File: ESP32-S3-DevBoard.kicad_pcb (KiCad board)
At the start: 4 copper layers, 32 x 57.1 mm, 27 parts, among them J1 USB_C_Receptacle_USB2.0_14P, J2 Conn_01x22_Socket, J3 Conn_01x22_Socket, SW1 SW_Push, SW2 SW_Push, U1 ESP32-S3-WROOM-1, U2 AMS1117-3.3

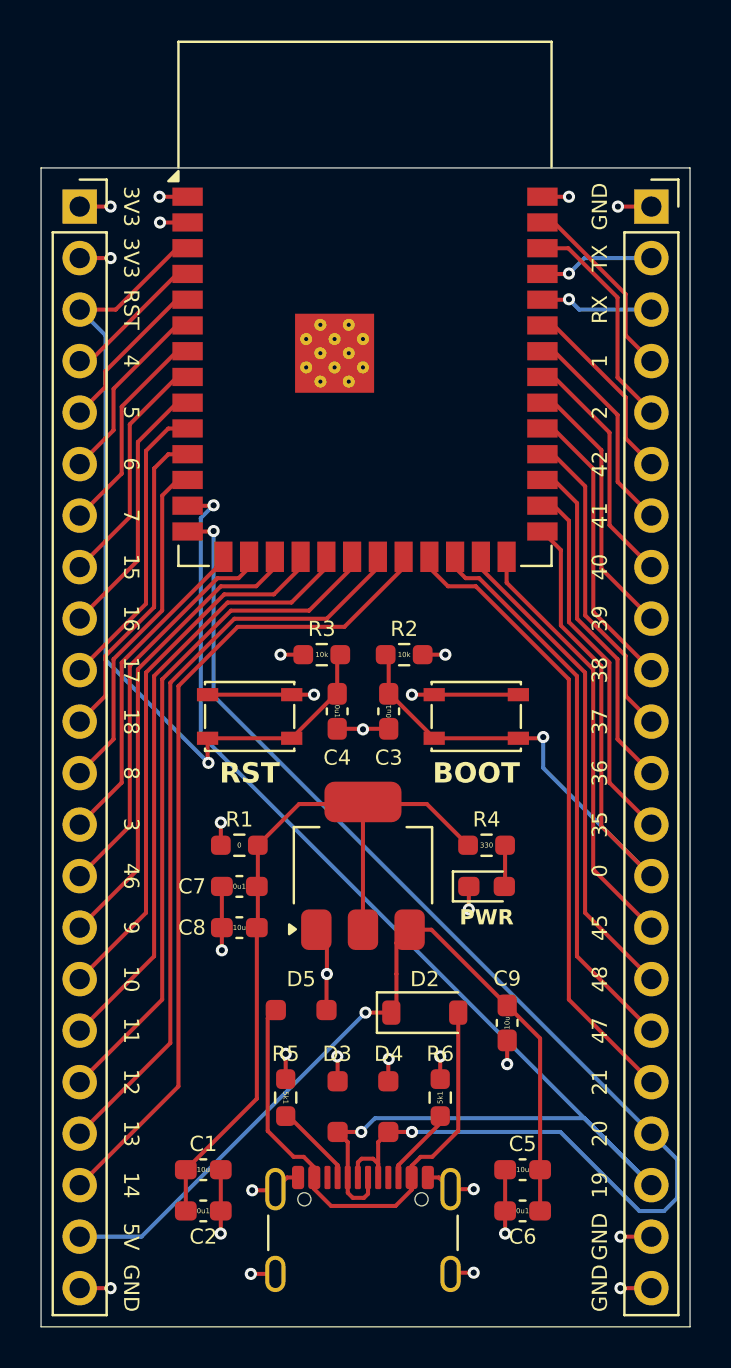
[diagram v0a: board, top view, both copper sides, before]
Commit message: Add impedance matching for USB lines
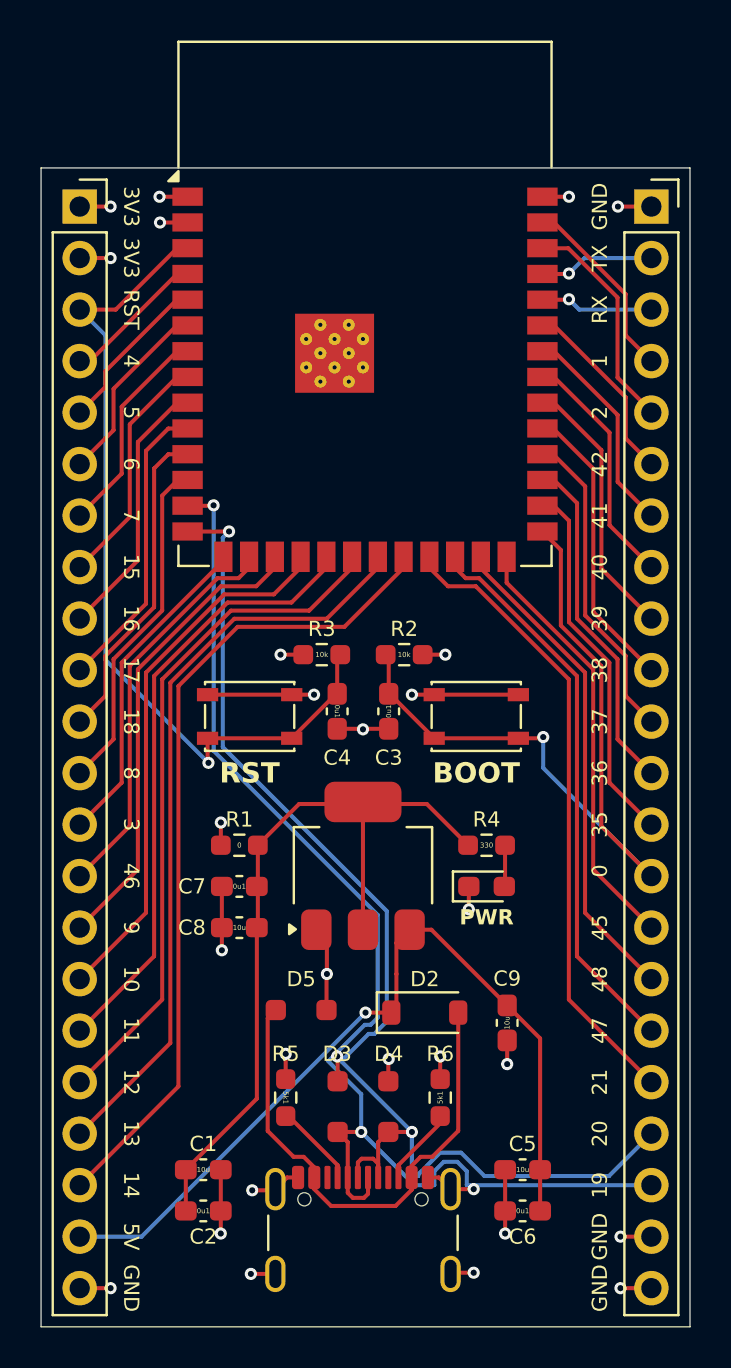
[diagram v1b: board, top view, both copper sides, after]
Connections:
- net GPIO_19 renamed D-
- net GPIO_20 renamed D+
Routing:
- net D-: track 66.6 -> 60.9 mm
- net D+: track 64.8 -> 59.6 mm
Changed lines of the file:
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@@
 	(net 42 "GPIO_21")
 	(net 43 "GPIO_47")
-	(net 44 "GPIO_19")
-	(net 45 "GPIO_20")
+	(net 44 "D-")
+	(net 45 "D+")
 	(footprint "Resistor_SMD:R_0603_1608Metric_Pad0.98x0.95mm_HandSolder"
 		(layer "F.Cu")
@@
 			(size 1.5 0.9)
 			(layers "F.Cu" "F.Paste" "F.Mask")
-			(net 44 "GPIO_19")
+			(net 44 "D-")
 			(pinfunction "IO19")
 			(pintype "bidirectional")
@@
 			(size 1.5 0.9)
 			(layers "F.Cu" "F.Paste" "F.Mask")
-			(net 45 "GPIO_20")
+			(net 45 "D+")
 			(pinfunction "IO20")
 			(pintype "bidirectional")
@@
 			(layers "*.Cu" "*.Mask")
 			(remove_unused_layers no)
-			(net 45 "GPIO_20")
+			(net 45 "D+")
 			(pinfunction "Pin_19")
 			(pintype "passive")
@@
 			(layers "*.Cu" "*.Mask")
 			(remove_unused_layers no)
-			(net 44 "GPIO_19")
+			(net 44 "D-")
 			(pinfunction "Pin_20")
 			(pintype "passive")
@@
 			(layers "F.Cu" "F.Paste" "F.Mask")
 			(roundrect_rratio 0.25)
-			(net 45 "GPIO_20")
+			(net 45 "D+")
 			(pinfunction "D+")
 			(pintype "bidirectional")
@@
 			(layers "F.Cu" "F.Paste" "F.Mask")
 			(roundrect_rratio 0.25)
-			(net 44 "GPIO_19")
+			(net 44 "D-")
 			(pinfunction "D-")
 			(pintype "bidirectional")
@@
 			(layers "F.Cu" "F.Paste" "F.Mask")
 			(roundrect_rratio 0.25)
-			(net 45 "GPIO_20")
+			(net 45 "D+")
 			(pinfunction "D+")
 			(pintype "bidirectional")
@@
 			(layers "F.Cu" "F.Paste" "F.Mask")
 			(roundrect_rratio 0.25)
-			(net 44 "GPIO_19")
+			(net 44 "D-")
 			(pinfunction "D-")
 			(pintype "bidirectional")
@@
 			(layers "F.Cu" "F.Paste" "F.Mask")
 			(roundrect_rratio 0.25)
-			(net 45 "GPIO_20")
+			(net 45 "D+")
 			(pinfunction "A1")
 			(pintype "passive")
@@
 			(layers "F.Cu" "F.Paste" "F.Mask")
 			(roundrect_rratio 0.25)
-			(net 44 "GPIO_19")
+			(net 44 "D-")
 			(pinfunction "A2")
 			(pintype "passive")
@@
 	)
 	(segment
-		(start 183.134 69.596)
-		(end 182.499 70.231)
+		(start 191.227 94.863529)
+		(end 190.875529 95.215)
 		(width 0.2)
 		(layer "B.Cu")
@@
 	)
 	(segment
-		(start 191.094 99.822)
-		(end 201.422 99.822)
+		(start 183.134 81.701471)
+		(end 191.227 89.794471)
 		(width 0.2)
 		(layer "B.Cu")
@@
 	)
 	(segment
-		(start 182.499 80.899)
-		(end 204.724 103.124)
+		(start 190.416 98.639397)
+		(end 190.416 100.5)
 		(width 0.2)
 		(layer "B.Cu")
@@
 	)
 	(segment
-		(start 201.422 99.822)
-		(end 204.724 103.124)
+		(start 193.04 103.124)
+		(end 194.02 103.124)
+		(width 0.2)
+		(layer "B.Cu")
+		(net 44)
+	)
+	(segment
+		(start 194.488629 101.971)
+		(end 195.151371 101.971)
 		(width 0.2)
 		(layer "B.Cu")
@@
 	)
 	(segment
-		(start 182.499 70.231)
-		(end 182.499 80.899)
+		(start 194.02 103.124)
+		(end 194.02 102.439629)
+		(width 0.2)
+		(layer "B.Cu")
+		(net 44)
+	)
+	(segment
+		(start 190.875529 95.215)
+		(end 190.592686 95.215)
+		(width 0.2)
+		(layer "B.Cu")
+		(net 44)
+	)
+	(segment
+		(start 194.02 102.439629)
+		(end 194.488629 101.971)
+		(width 0.2)
+		(layer "B.Cu")
+		(net 44)
+	)
+	(segment
+		(start 190.592686 95.215)
+		(end 188.792145 97.015542)
+		(width 0.2)
+		(layer "B.Cu")
+		(net 44)
+	)
+	(segment
+		(start 188.792145 97.015542)
+		(end 190.416 98.639397)
 		(width 0.2)
 		(layer "B.Cu")
@@
 	(segment
 		(start 190.416 100.5)
-		(end 191.094 99.822)
+		(end 193.04 103.124)
 		(width 0.2)
 		(layer "B.Cu")
@@
 	)
 	(segment
-		(start 191.25 102.069295)
-		(end 191.25 102.746)
+		(start 195.62 103.124)
+		(end 204.724 103.124)
 		(width 0.2)
-		(layer "F.Cu")
-		(net 45)
+		(layer "B.Cu")
+		(net 44)
+	)
+	(segment
+		(start 191.227 89.794471)
+		(end 191.227 94.863529)
+		(width 0.2)
+		(layer "B.Cu")
+		(net 44)
+	)
+	(segment
+		(start 183.134 69.596)
+		(end 183.134 81.701471)
+		(width 0.2)
+		(layer "B.Cu")
+		(net 44)
+	)
+	(segment
+		(start 195.62 102.439629)
+		(end 195.62 103.124)
+		(width 0.2)
+		(layer "B.Cu")
+		(net 44)
+	)
+	(segment
+		(start 195.151371 101.971)
+		(end 195.62 102.439629)
+		(width 0.2)
+		(layer "B.Cu")
+		(net 44)
 	)
 	(segment
-		(start 181.85 70.89)
-		(end 183.11 70.89)
+		(start 191.25 102.069295)
+		(end 191.25 102.746)
 		(width 0.2)
 		(layer "F.Cu")
@@
 	)
 	(segment
+		(start 183.891998 70.89)
+		(end 181.85 70.89)
+		(width 0.2)
+		(layer "F.Cu")
+		(net 45)
+	)
+	(segment
 		(start 190.430705 101.819295)
 		(end 191 101.819295)
@@
 	)
 	(segment
-		(start 183.11 70.89)
-		(end 183.134 70.866)
+		(start 183.896 70.885998)
+		(end 183.891998 70.89)
 		(width 0.2)
 		(layer "F.Cu")
@@
 	)
 	(via
-		(at 183.134 70.866)
+		(at 183.896 70.885998)
 		(size 0.6)
 		(drill 0.3)
@@
 	)
 	(segment
-		(start 204.133654 104.4)
-		(end 205.35 104.4)
+		(start 191.061917 95.66498)
+		(end 190.779074 95.66498)
 		(width 0.2)
 		(layer "B.Cu")
@@
 	)
 	(segment
-		(start 183.134 78.994)
+		(start 192.913 102.360603)
+		(end 193.226396 102.673999)
+		(width 0.2)
+		(layer "B.Cu")
+		(net 45)
+	)
+	(segment
+		(start 195.337759 101.52102)
+		(end 196.490738 102.673999)
+		(width 0.2)
+		(layer "B.Cu")
+		(net 45)
+	)
+	(segment
+		(start 202.634001 102.673999)
 		(end 204.724 100.584)
 		(width 0.2)
@@
 	)
 	(segment
-		(start 192.913 100.5)
-		(end 200.233654 100.5)
+		(start 190.779074 95.66498)
+		(end 189.428527 97.015527)
 		(width 0.2)
 		(layer "B.Cu")
@@
 	)
 	(segment
-		(start 206 103.75)
-		(end 206 101.86)
+		(start 183.584001 81.515104)
+		(end 191.67698 89.608083)
 		(width 0.2)
 		(layer "B.Cu")
@@
 	)
 	(segment
-		(start 183.134 70.866)
-		(end 183.134 78.994)
+		(start 196.490738 102.673999)
+		(end 202.634001 102.673999)
 		(width 0.2)
 		(layer "B.Cu")
@@
 	)
 	(segment
-		(start 200.233654 100.5)
-		(end 204.133654 104.4)
+		(start 193.226396 102.673999)
+		(end 193.226396 102.596865)
 		(width 0.2)
 		(layer "B.Cu")
@@
 	)
 	(segment
-		(start 205.35 104.4)
-		(end 206 103.75)
+		(start 193.226396 102.596865)
+		(end 194.302241 101.52102)
 		(width 0.2)
 		(layer "B.Cu")
@@
 	)
 	(segment
-		(start 206 101.86)
-		(end 204.724 100.584)
+		(start 194.302241 101.52102)
+		(end 195.337759 101.52102)
+		(width 0.2)
+		(layer "B.Cu")
+		(net 45)
+	)
+	(segment
+		(start 183.584001 71.197997)
+		(end 183.584001 81.515104)
+		(width 0.2)
+		(layer "B.Cu")
+		(net 45)
+	)
+	(segment
+		(start 189.428527 97.015527)
+		(end 192.913 100.5)
+		(width 0.2)
+		(layer "B.Cu")
+		(net 45)
+	)
+	(segment
+		(start 191.67698 89.608083)
+		(end 191.67698 95.049917)
+		(width 0.2)
+		(layer "B.Cu")
+		(net 45)
+	)
+	(segment
+		(start 192.913 100.5)
+		(end 192.913 102.360603)
+		(width 0.2)
+		(layer "B.Cu")
+		(net 45)
+	)
+	(segment
+		(start 183.896 70.885998)
+		(end 183.584001 71.197997)
+		(width 0.2)
+		(layer "B.Cu")
+		(net 45)
+	)
+	(segment
+		(start 191.67698 95.049917)
+		(end 191.061917 95.66498)
 		(width 0.2)
 		(layer "B.Cu")

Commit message: Create gerber files
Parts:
- added G***: LOGO, Footprints:ER, F.Cu at (182.6, 95.4)
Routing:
- net VCC_5V: track 42.1 -> 49.1 mm
- net D-: track 60.9 -> 58.7 mm
- net D+: track 59.6 -> 58.4 mm
